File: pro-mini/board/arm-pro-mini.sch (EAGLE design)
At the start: 55 parts, among them J1 USB, J2 SWD HEADER, Q1 12Mhz, T1 DTA114EET1G (2 X 10K), U1 MCP1754ST-3302E/CB, U2 NUF2042XV6T1G, U3 LPC11U35FHI33/501

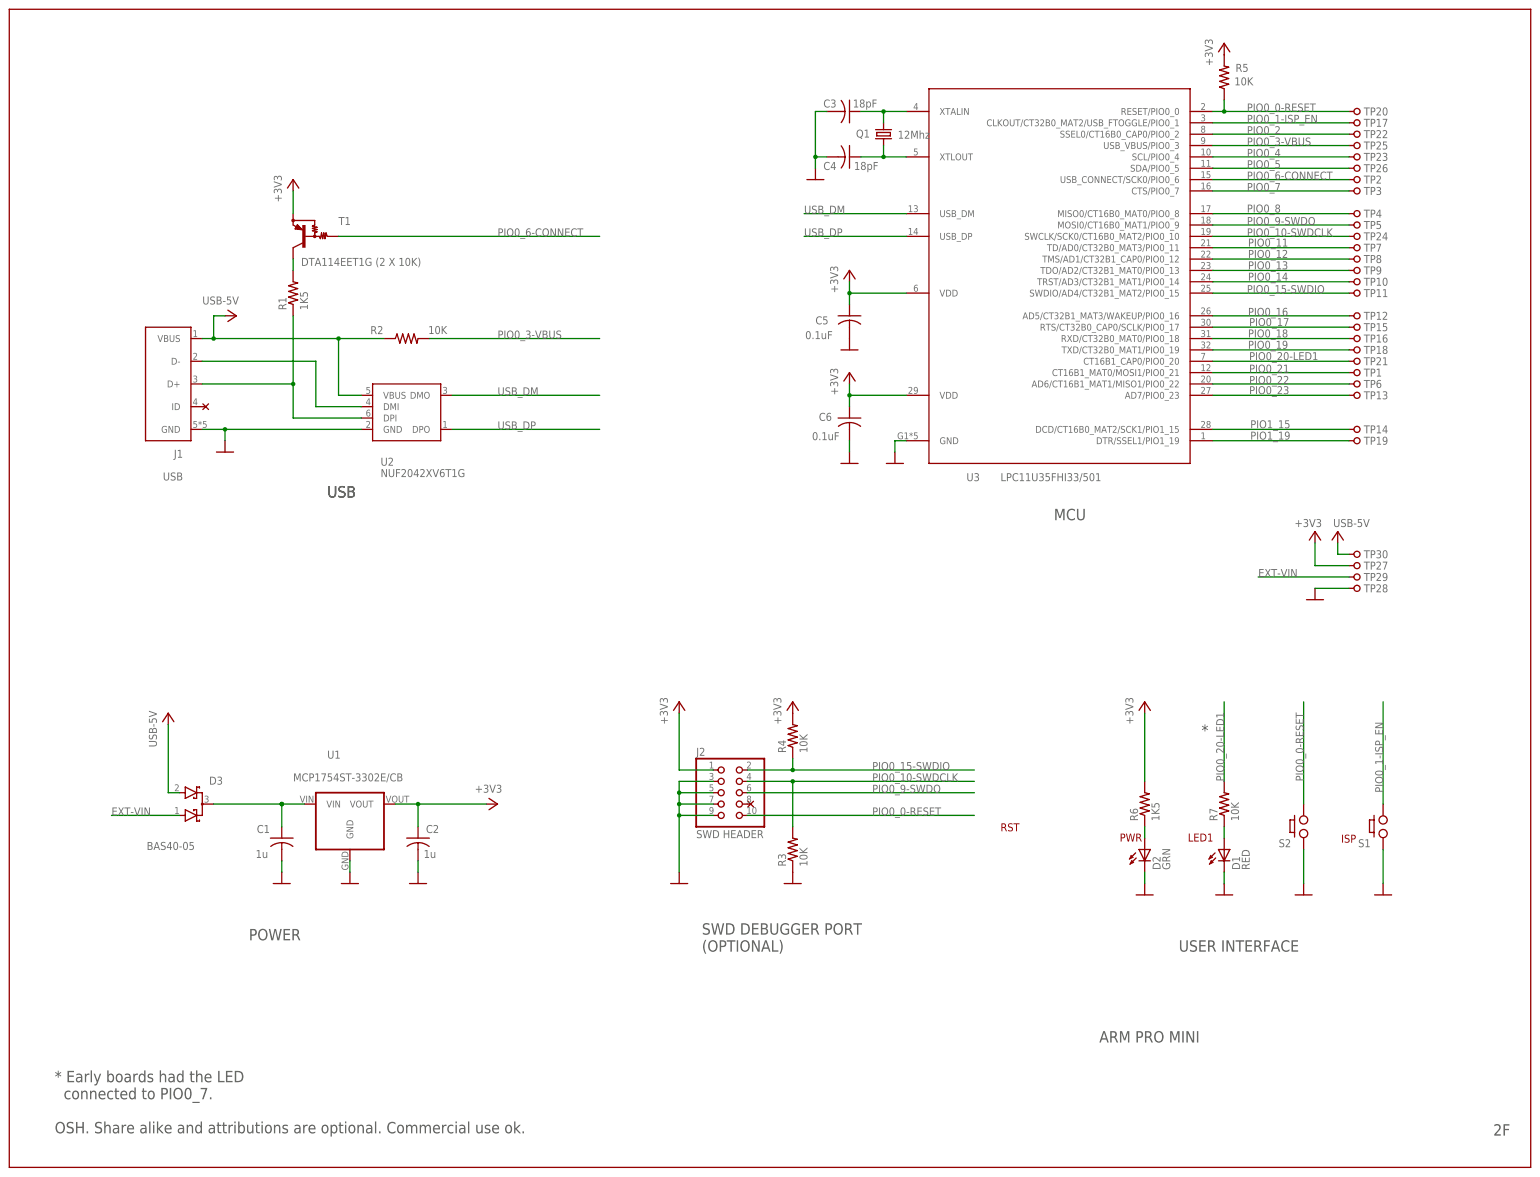
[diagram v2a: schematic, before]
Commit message: Added diodes/cap circuit for a single button ISP. Grounded two extra pins of the crystal. Swapped the order and increase the spacing between the two buttons. Ready for final auto routing.
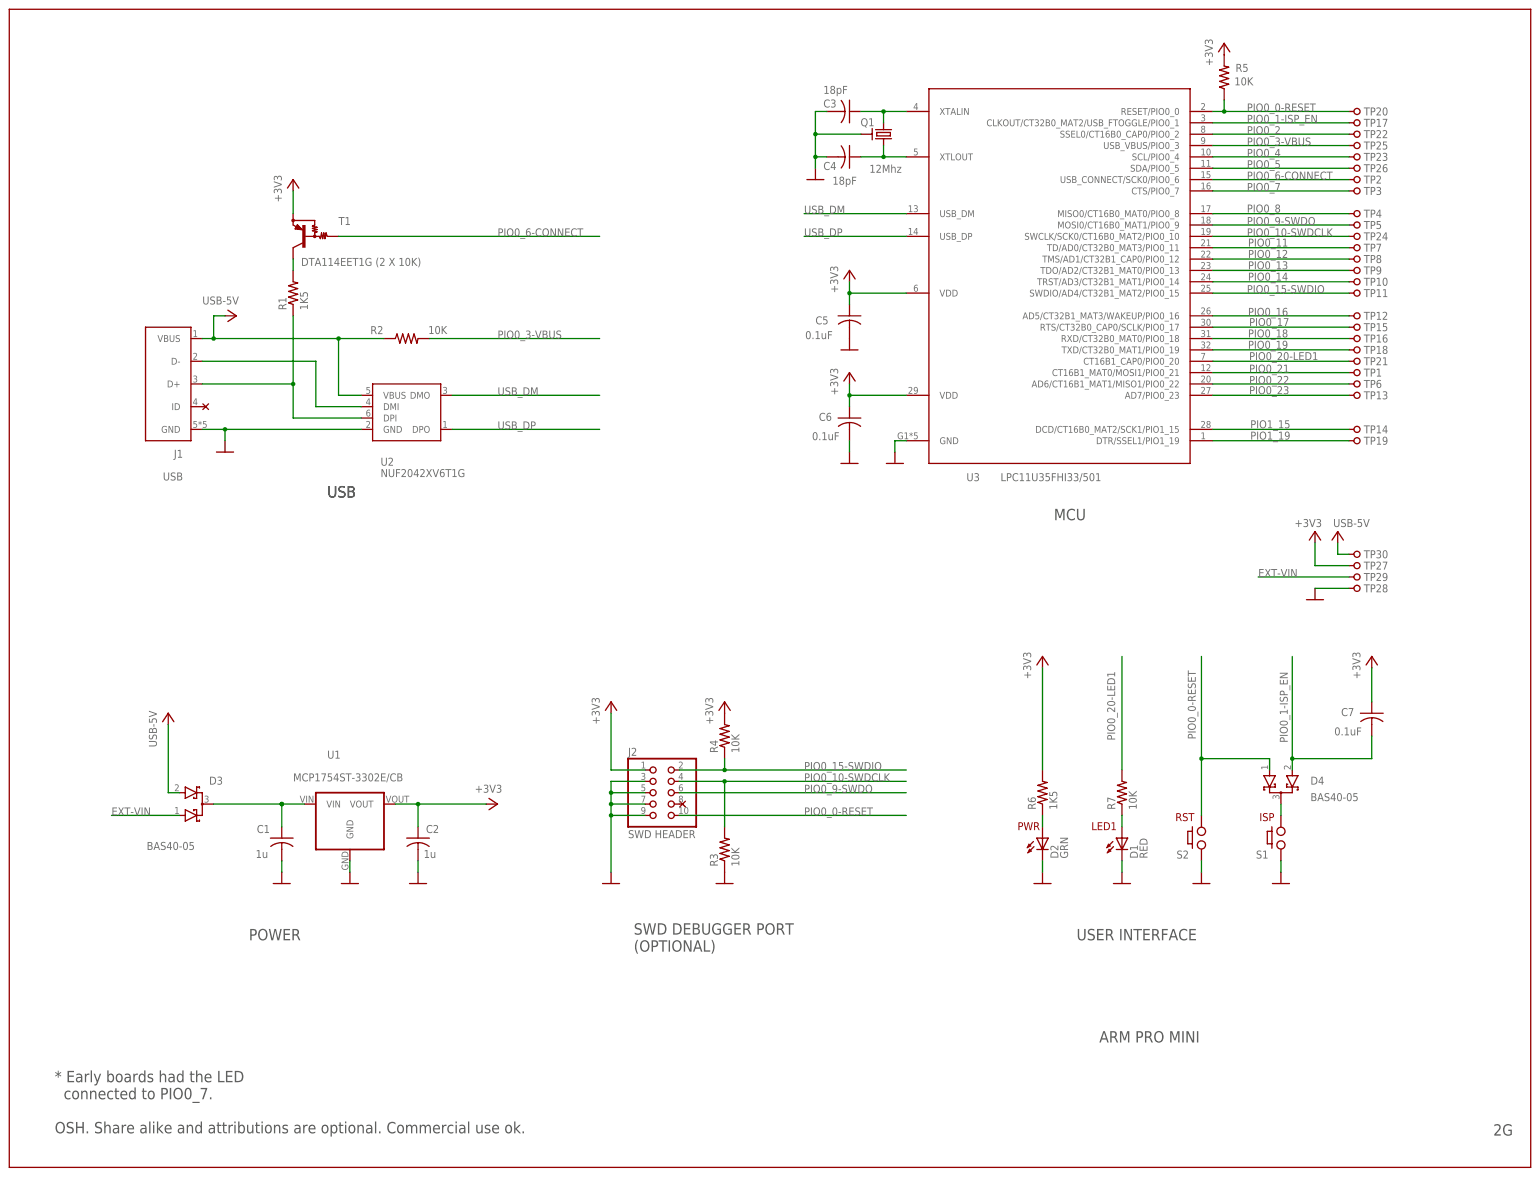
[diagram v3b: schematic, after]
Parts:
- added C7: 0.1uF, arm-pro-mini:CAPACITORC0603K
- added D4: BAS40-05, arm-pro-mini:BAS40-05
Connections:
- new net N$8: D4.C, S1.2
- net +3V3: now also C7.1
- net GND: now also Q1.GND
- net PIO0_0-RESET: now also D4.A1
- net PIO0_1-ISP_EN: now also C7.2, D4.A2; no longer S1.2
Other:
- note added: "2G"
- note removed: "*"
- note removed: "2F"
- moved on the sheet: D1, D2, J2, R3, R4, R6, R7, S1, S2

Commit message: Performed final auto routing.
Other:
- moved on the sheet: C7, D4, S1, S2
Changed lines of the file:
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@@
 <text x="139.7" y="48.26" size="2.54" layer="97">SWD DEBUGGER PORT
 (OPTIONAL)</text>
-<text x="279.654" y="77.47" size="1.778" layer="94">ISP</text>
-<text x="260.858" y="77.47" size="1.778" layer="94">RST</text>
+<text x="279.654" y="72.39" size="1.778" layer="94">ISP</text>
+<text x="300.99" y="72.644" size="1.778" layer="94">RST</text>
 <text x="242.062" y="75.438" size="1.778" layer="94">LED1</text>
 <text x="225.552" y="75.438" size="1.778" layer="94">PWR</text>
@@
 <instance part="U$3" gate="G$1" x="43.18" y="170.18" rot="R180"/>
 <instance part="U$20" gate="G$1" x="238.76" y="0"/>
-<instance part="GND22" gate="1" x="284.48" y="63.5"/>
-<instance part="S1" gate="G$1" x="284.48" y="73.66" smashed="yes">
-<attribute name="NAME" x="278.892" y="69.088" size="1.778" layer="95"/>
+<instance part="GND22" gate="1" x="289.56" y="63.5"/>
+<instance part="S1" gate="G$1" x="289.56" y="73.66" smashed="yes">
+<attribute name="NAME" x="283.972" y="69.088" size="1.778" layer="95"/>
 </instance>
 <instance part="GND3" gate="1" x="76.2" y="63.5"/>
@@
 </instance>
 <instance part="+3V8" gate="G$1" x="271.78" y="251.46"/>
-<instance part="S2" gate="G$1" x="266.7" y="73.66" smashed="yes">
-<attribute name="NAME" x="261.112" y="69.088" size="1.778" layer="95"/>
-</instance>
-<instance part="GND14" gate="1" x="266.7" y="63.5"/>
+<instance part="S2" gate="G$1" x="309.88" y="73.66" smashed="yes">
+<attribute name="NAME" x="304.292" y="69.088" size="1.778" layer="95"/>
+</instance>
+<instance part="GND14" gate="1" x="309.88" y="63.5"/>
 <instance part="R2" gate="G$1" x="88.9" y="185.42" smashed="yes">
 <attribute name="NAME" x="80.772" y="186.4106" size="1.778" layer="95"/>
@@
 <instance part="J1" gate="G$1" x="35.56" y="170.18"/>
 <instance part="U2" gate="G$1" x="88.9" y="167.64"/>
-<instance part="D4" gate="G$1" x="284.48" y="86.36" smashed="yes" rot="MR270">
-<attribute name="NAME" x="291.084" y="87.4014" size="1.778" layer="95" rot="MR180"/>
-<attribute name="VALUE" x="291.084" y="83.7184" size="1.778" layer="96" rot="MR180"/>
-</instance>
-<instance part="C7" gate="G$1" x="304.8" y="101.6" smashed="yes">
-<attribute name="NAME" x="297.942" y="100.965" size="1.778" layer="95"/>
-<attribute name="VALUE" x="296.418" y="96.647" size="1.778" layer="96"/>
-</instance>
-<instance part="+3V10" gate="G$1" x="304.8" y="114.3"/>
+<instance part="D4" gate="G$1" x="289.56" y="86.36" smashed="yes" rot="R270">
+<attribute name="NAME" x="282.956" y="87.4014" size="1.778" layer="95" rot="R180"/>
+<attribute name="VALUE" x="282.956" y="83.7184" size="1.778" layer="96" rot="R180"/>
+</instance>
+<instance part="C7" gate="G$1" x="269.24" y="101.6" smashed="yes">
+<attribute name="NAME" x="262.382" y="100.965" size="1.778" layer="95"/>
+<attribute name="VALUE" x="260.858" y="96.647" size="1.778" layer="96"/>
+</instance>
+<instance part="+3V10" gate="G$1" x="269.24" y="114.3"/>
 </instances>
 <busses>
@@
 <segment>
 <pinref part="GND22" gate="1" pin="GND"/>
-<wire x1="284.48" y1="66.04" x2="284.48" y2="68.58" width="0.1524" layer="91"/>
+<wire x1="289.56" y1="66.04" x2="289.56" y2="68.58" width="0.1524" layer="91"/>
 <pinref part="S1" gate="G$1" pin="1"/>
 </segment>
@@
 <pinref part="GND14" gate="1" pin="GND"/>
 <pinref part="S2" gate="G$1" pin="1"/>
-<wire x1="266.7" y1="66.04" x2="266.7" y2="68.58" width="0.1524" layer="91"/>
+<wire x1="309.88" y1="66.04" x2="309.88" y2="68.58" width="0.1524" layer="91"/>
 </segment>
 <segment>
@@
 <segment>
 <pinref part="C7" gate="G$1" pin="1"/>
-<wire x1="304.8" y1="104.14" x2="304.8" y2="111.76" width="0.1524" layer="91"/>
+<wire x1="269.24" y1="104.14" x2="269.24" y2="111.76" width="0.1524" layer="91"/>
 <pinref part="+3V10" gate="G$1" pin="+3V3"/>
 </segment>
@@
 <segment>
 <pinref part="S2" gate="G$1" pin="2"/>
-<wire x1="266.7" y1="78.74" x2="266.7" y2="91.44" width="0.1524" layer="91"/>
-<label x="265.43" y="95.758" size="1.778" layer="95" rot="R90"/>
-<wire x1="266.7" y1="91.44" x2="266.7" y2="114.3" width="0.1524" layer="91"/>
-<wire x1="281.94" y1="91.44" x2="266.7" y2="91.44" width="0.1524" layer="91"/>
-<junction x="266.7" y="91.44"/>
+<wire x1="309.88" y1="78.74" x2="309.88" y2="91.44" width="0.1524" layer="91"/>
+<label x="308.61" y="98.298" size="1.778" layer="95" rot="R90"/>
+<wire x1="309.88" y1="91.44" x2="309.88" y2="116.84" width="0.1524" layer="91"/>
+<wire x1="292.1" y1="91.44" x2="309.88" y2="91.44" width="0.1524" layer="91"/>
+<junction x="309.88" y="91.44"/>
 <pinref part="D4" gate="G$1" pin="A1"/>
-<wire x1="281.94" y1="88.9" x2="281.94" y2="91.44" width="0.1524" layer="91"/>
+<wire x1="292.1" y1="88.9" x2="292.1" y2="91.44" width="0.1524" layer="91"/>
 </segment>
 </net>
@@
 <pinref part="C7" gate="G$1" pin="2"/>
 <wire x1="287.02" y1="91.44" x2="287.02" y2="114.3" width="0.1524" layer="91"/>
-<wire x1="287.02" y1="91.44" x2="304.8" y2="91.44" width="0.1524" layer="91"/>
-<wire x1="304.8" y1="91.44" x2="304.8" y2="96.52" width="0.1524" layer="91"/>
+<wire x1="287.02" y1="91.44" x2="269.24" y2="91.44" width="0.1524" layer="91"/>
+<wire x1="269.24" y1="91.44" x2="269.24" y2="96.52" width="0.1524" layer="91"/>
 <pinref part="D4" gate="G$1" pin="A2"/>
 <wire x1="287.02" y1="88.9" x2="287.02" y2="91.44" width="0.1524" layer="91"/>
@@
 <pinref part="S1" gate="G$1" pin="2"/>
 <pinref part="D4" gate="G$1" pin="C"/>
-<wire x1="284.48" y1="81.28" x2="284.48" y2="78.74" width="0.1524" layer="91"/>
-</segment>
-</net>
+<wire x1="289.56" y1="81.28" x2="289.56" y2="78.74" width="0.1524" layer="91"/>
+</segment>
+</net>

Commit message: Bumped version number to 3. Tweaked labels.
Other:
- note added: "3"
- note removed: "2G"
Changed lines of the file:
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@@
 <wire x1="0" y1="0" x2="0" y2="259.08" width="0.1524" layer="94"/>
 <text x="233.68" y="144.78" size="2.54" layer="97">MCU</text>
-<text x="331.978" y="7.112" size="2.54" layer="97">2G</text>
+<text x="331.978" y="7.112" size="2.54" layer="97">3</text>
 <text x="71.12" y="149.86" size="2.54" layer="97">USB</text>
 <text x="139.7" y="48.26" size="2.54" layer="97">SWD DEBUGGER PORT

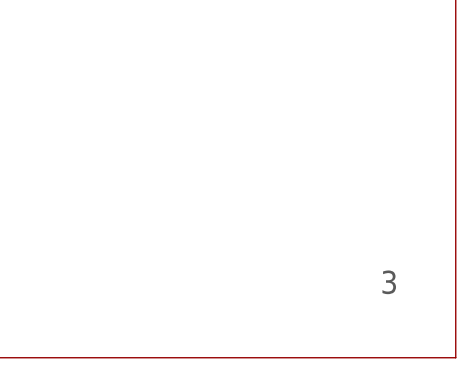
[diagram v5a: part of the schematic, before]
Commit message: Added vias to switch pads for added mechanicam support. Removed the solder stop of the 4 vias under the MCU. No electrical or stencil change.
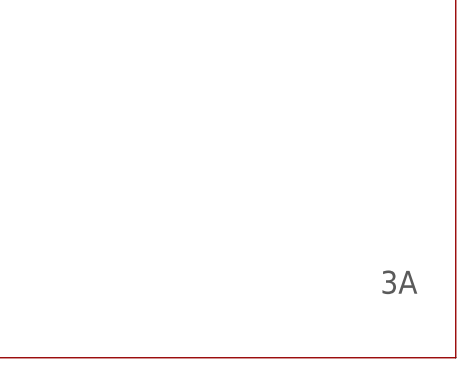
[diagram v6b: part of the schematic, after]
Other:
- note added: "3A"
- note removed: "3"
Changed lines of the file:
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@@
 <wire x1="0" y1="0" x2="0" y2="259.08" width="0.1524" layer="94"/>
 <text x="233.68" y="144.78" size="2.54" layer="97">MCU</text>
-<text x="331.978" y="7.112" size="2.54" layer="97">3</text>
+<text x="331.978" y="7.112" size="2.54" layer="97">3A</text>
 <text x="71.12" y="149.86" size="2.54" layer="97">USB</text>
 <text x="139.7" y="48.26" size="2.54" layer="97">SWD DEBUGGER PORT

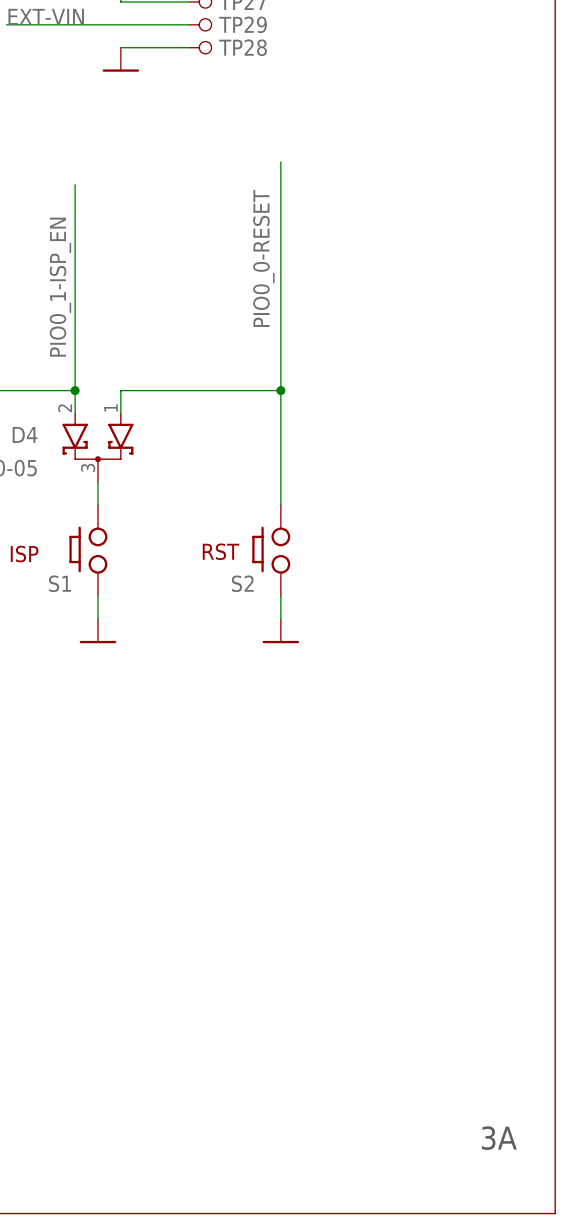
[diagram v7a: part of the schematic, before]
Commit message: Minor tweaks, extended pads of the crystial, transistor and USB connector for easier hand soldering. Fixed 'ARM MINI PRO' label to 'ARM PRO MINI'. Most Had to move the crystal a little bit so existing stencils from version 3A may or may not fit this new version 3B.
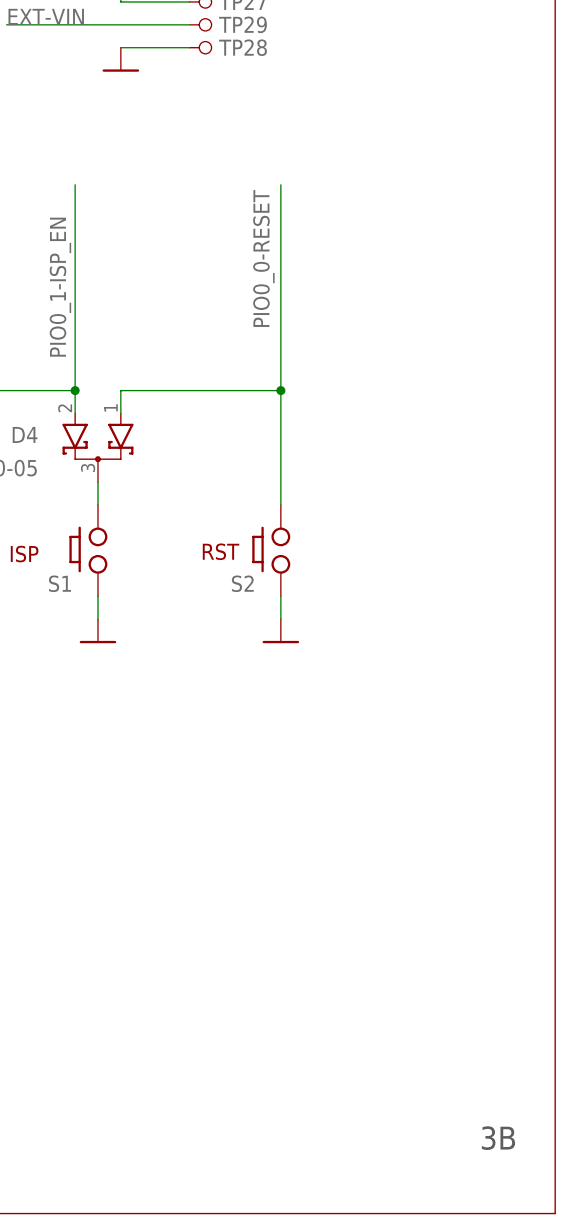
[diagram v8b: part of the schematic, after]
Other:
- note added: "3B"
- note removed: "3A"
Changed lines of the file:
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@@
 <wire x1="0" y1="0" x2="0" y2="259.08" width="0.1524" layer="94"/>
 <text x="233.68" y="144.78" size="2.54" layer="97">MCU</text>
-<text x="331.978" y="7.112" size="2.54" layer="97">3A</text>
+<text x="331.978" y="7.112" size="2.54" layer="97">3B</text>
 <text x="71.12" y="149.86" size="2.54" layer="97">USB</text>
 <text x="139.7" y="48.26" size="2.54" layer="97">SWD DEBUGGER PORT
@@
 <wire x1="309.88" y1="78.74" x2="309.88" y2="91.44" width="0.1524" layer="91"/>
 <label x="308.61" y="98.298" size="1.778" layer="95" rot="R90"/>
-<wire x1="309.88" y1="91.44" x2="309.88" y2="116.84" width="0.1524" layer="91"/>
+<wire x1="309.88" y1="91.44" x2="309.88" y2="114.3" width="0.1524" layer="91"/>
 <wire x1="292.1" y1="91.44" x2="309.88" y2="91.44" width="0.1524" layer="91"/>
 <junction x="309.88" y="91.44"/>
